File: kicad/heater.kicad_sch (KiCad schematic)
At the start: 3 parts, among them Q1 AO3400A

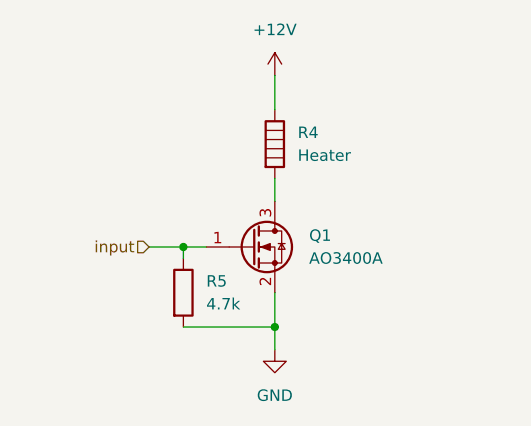
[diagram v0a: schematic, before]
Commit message: added connectors to schematic
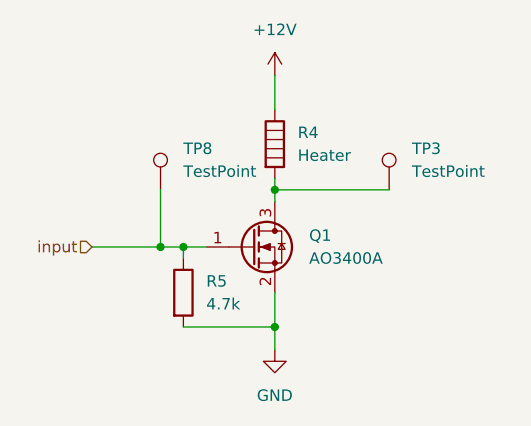
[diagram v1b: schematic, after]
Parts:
- added TP3, TP8: TestPoint, symbol Connector:TestPoint
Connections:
- net input: now also TP8.1
- net at Q1.3 (D), R4.2: now also TP3.1
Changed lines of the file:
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@@
+	)
+	(junction
+		(at 78.74 86.36)
+		(diameter 0)
+		(color 0 0 0 0)
+	)
+	(junction
+		(at 91.44 80.01)
+		(diameter 0)
+		(color 0 0 0 0)
 	)
 	(junction
@@
 	(wire
 		(pts
-			(xy 91.44 78.74) (xy 91.44 81.28)
+			(xy 91.44 78.74) (xy 91.44 80.01)
+		)
+		(stroke
+			(width 0)
+			(type default)
+		)
+	)
+	(wire
+		(pts
+			(xy 78.74 86.36) (xy 81.28 86.36)
 		)
 		(stroke
@@
 	(wire
 		(pts
+			(xy 91.44 80.01) (xy 104.14 80.01)
+		)
+		(stroke
+			(width 0)
+			(type default)
+		)
+	)
+	(wire
+		(pts
 			(xy 81.28 95.25) (xy 91.44 95.25)
 		)
@@
 	(wire
 		(pts
-			(xy 77.47 86.36) (xy 81.28 86.36)
+			(xy 78.74 80.01) (xy 78.74 86.36)
+		)
+		(stroke
+			(width 0)
+			(type default)
+		)
+	)
+	(wire
+		(pts
+			(xy 91.44 80.01) (xy 91.44 81.28)
+		)
+		(stroke
+			(width 0)
+			(type default)
+		)
+	)
+	(wire
+		(pts
+			(xy 71.12 86.36) (xy 78.74 86.36)
 		)
 		(stroke
@@
 	(hierarchical_label "input"
 		(shape input)
-		(at 77.47 86.36 180)
+		(at 71.12 86.36 180)
 		(effects
 			(font
@@
 	)
 	(symbol
+		(lib_id "Connector:TestPoint")
+		(at 78.74 80.01 0)
+		(unit 1)
+		(exclude_from_sim no)
+		(in_bom yes)
+		(on_board yes)
+		(dnp no)
+		(fields_autoplaced yes)
+		(property "Reference" "TP8"
+			(at 81.28 75.4379 0)
+			(effects
+				(font
+					(size 1.27 1.27)
+				)
+				(justify left)
+			)
+		)
+		(property "Value" "TestPoint"
+			(at 81.28 77.9779 0)
+			(effects
+				(font
+					(size 1.27 1.27)
+				)
+				(justify left)
+			)
+		)
+		(property "Footprint" ""
+			(at 83.82 80.01 0)
+			(effects
+				(font
+					(size 1.27 1.27)
+				)
+				(hide yes)
+			)
+		)
+		(property "Datasheet" "~"
+			(at 83.82 80.01 0)
+			(effects
+				(font
+					(size 1.27 1.27)
+				)
+				(hide yes)
+			)
+		)
+		(property "Description" "test point"
+			(at 78.74 80.01 0)
+			(effects
+				(font
+					(size 1.27 1.27)
+				)
+				(hide yes)
+			)
+		)
+		(pin "1"
+		)
+		(instances
+			(project ""
+				(path "/99399f2a-756c-4718-9b6a-bb37855e6538/1d219fe6-bc63-44d7-97db-56de52b65009"
+					(reference "TP8")
+					(unit 1)
+				)
+				(path "/99399f2a-756c-4718-9b6a-bb37855e6538/35c344b1-4964-4b72-be4c-fe15a9a01785"
+					(reference "TP10")
+					(unit 1)
+				)
+				(path "/99399f2a-756c-4718-9b6a-bb37855e6538/d6c312da-2fd3-41bb-8abb-f867abf702cd"
+					(reference "TP9")
+					(unit 1)
+				)
+				(path "/99399f2a-756c-4718-9b6a-bb37855e6538/d96b2377-b712-43b7-b059-2b3612144cdd"
+					(reference "TP11")
+					(unit 1)
+				)
+				(path "/99399f2a-756c-4718-9b6a-bb37855e6538/fa44cc0c-94de-4677-8c40-03642583747f"
+					(reference "TP12")
+					(unit 1)
+				)
+			)
+		)
+	)
+	(symbol
 		(lib_id "Device:R")
 		(at 81.28 91.44 0)
@@
 					(unit 1)
 				)
+			)
+		)
+	)
+	(symbol
+		(lib_id "Connector:TestPoint")
+		(at 104.14 80.01 0)
+		(unit 1)
+		(exclude_from_sim no)
+		(in_bom yes)
+		(on_board yes)
+		(dnp no)
+		(fields_autoplaced yes)
+		(property "Reference" "TP3"
+			(at 106.68 75.4379 0)
+			(effects
+				(font
+					(size 1.27 1.27)
+				)
+				(justify left)
+			)
+		)
+		(property "Value" "TestPoint"
+			(at 106.68 77.9779 0)
+			(effects
+				(font
+					(size 1.27 1.27)
+				)
+				(justify left)
+			)
+		)
+		(property "Footprint" ""
+			(at 109.22 80.01 0)
+			(effects
+				(font
+					(size 1.27 1.27)
+				)
+				(hide yes)
+			)
+		)
+		(property "Datasheet" "~"
+			(at 109.22 80.01 0)
+			(effects
+				(font
+					(size 1.27 1.27)
+				)
+				(hide yes)
+			)
+		)
+		(property "Description" "test point"
+			(at 104.14 80.01 0)
+			(effects
+				(font
+					(size 1.27 1.27)
+				)
+				(hide yes)
+			)
+		)
+		(pin "1"
+		)
+		(instances
+			(project ""
+				(path "/99399f2a-756c-4718-9b6a-bb37855e6538/1d219fe6-bc63-44d7-97db-56de52b65009"
+					(reference "TP3")
+					(unit 1)
+				)
+				(path "/99399f2a-756c-4718-9b6a-bb37855e6538/35c344b1-4964-4b72-be4c-fe15a9a01785"
+					(reference "TP5")
+					(unit 1)
+				)
+				(path "/99399f2a-756c-4718-9b6a-bb37855e6538/d6c312da-2fd3-41bb-8abb-f867abf702cd"
+					(reference "TP4")
+					(unit 1)
+				)
+				(path "/99399f2a-756c-4718-9b6a-bb37855e6538/d96b2377-b712-43b7-b059-2b3612144cdd"
+					(reference "TP6")
+					(unit 1)
+				)
+				(path "/99399f2a-756c-4718-9b6a-bb37855e6538/fa44cc0c-94de-4677-8c40-03642583747f"
+					(reference "TP7")
+					(unit 1)
+				)

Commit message: added footprints
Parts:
- TP3, TP8: footprint (none) -> TestPoint:TestPoint_Pad_D2.5mm
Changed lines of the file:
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@@
 			)
 		)
-		(property "Footprint" ""
+		(property "Footprint" "TestPoint:TestPoint_Pad_D2.5mm"
 			(at 83.82 80.01 0)
 			(effects
@@
 			)
 		)
-		(property "Footprint" ""
+		(property "Footprint" "TestPoint:TestPoint_Pad_D2.5mm"
 			(at 109.22 80.01 0)
 			(effects
